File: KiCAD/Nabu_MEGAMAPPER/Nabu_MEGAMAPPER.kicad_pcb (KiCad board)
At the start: 2 copper layers, 41 parts, among them J1 Z80 Socket Header, J2 Z80 Socket Header, J3 JTAG, U1 Z80CPU, U10 74LS374, U11 74LS374, U12 74LS85, U13 XC9536PC44, U14 74LS139, U15 AS6C4008-55PCN, U16 AS6C4008-55PCN, U17 AS6C4008-55PCN, U18 AS6C4008-55PCN, U19 74LS245, U2 74LS32, U3 74LS670, U4 74LS670, U5 HM6116, U6 74LS157, U7 74LS157, U8 74LS157, U9 74LS244

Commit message: Continued work on PCB layout
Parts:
- moved J3 291.6 mm to (225.4, 78.1), turned to 180 degrees
- moved U15 271.8 mm to (139.7, 108.0)
- moved U5 269.7 mm to (207.6, 118.1)
- moved U9 267.7 mm to (167.0, 87.0), turned to 90 degrees
- moved C5 266.0 mm to (217.8, 114.9), turned to 180 degrees
- moved U19 255.8 mm to (186.7, 111.1)
- moved U2 246.0 mm to (167.0, 73.0), turned to 90 degrees
- moved C13 240.5 mm to (200.0, 92.7), turned to 90 degrees
- moved U16 234.0 mm to (118.1, 108.0)
- moved U10 223.9 mm to (134.0, 87.0), turned to 90 degrees
- moved C19 219.8 mm to (188.0, 107.9)
- moved C1 214.5 mm to (166.4, 94.6)
- moved U11 213.6 mm to (134.0, 73.0), turned to 90 degrees
- moved C2 213.6 mm to (163.8, 66.7), turned to -90 degrees
- moved U8 212.4 mm to (134.0, 101.0), turned to 90 degrees
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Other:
- board outline added: 156.8 x 86.4 mm
- board text added: "+5V"
- board text added: "GND"
- board text added: "Gavin Tersteeg, 2024"
- board text added: "Rev. 0"
- board text added: "TCK"
- board text added: "TDI"
- board text added: "TDO"
- board text added: "TMS"
- board text added: "Z80 MEGAMAPPER"

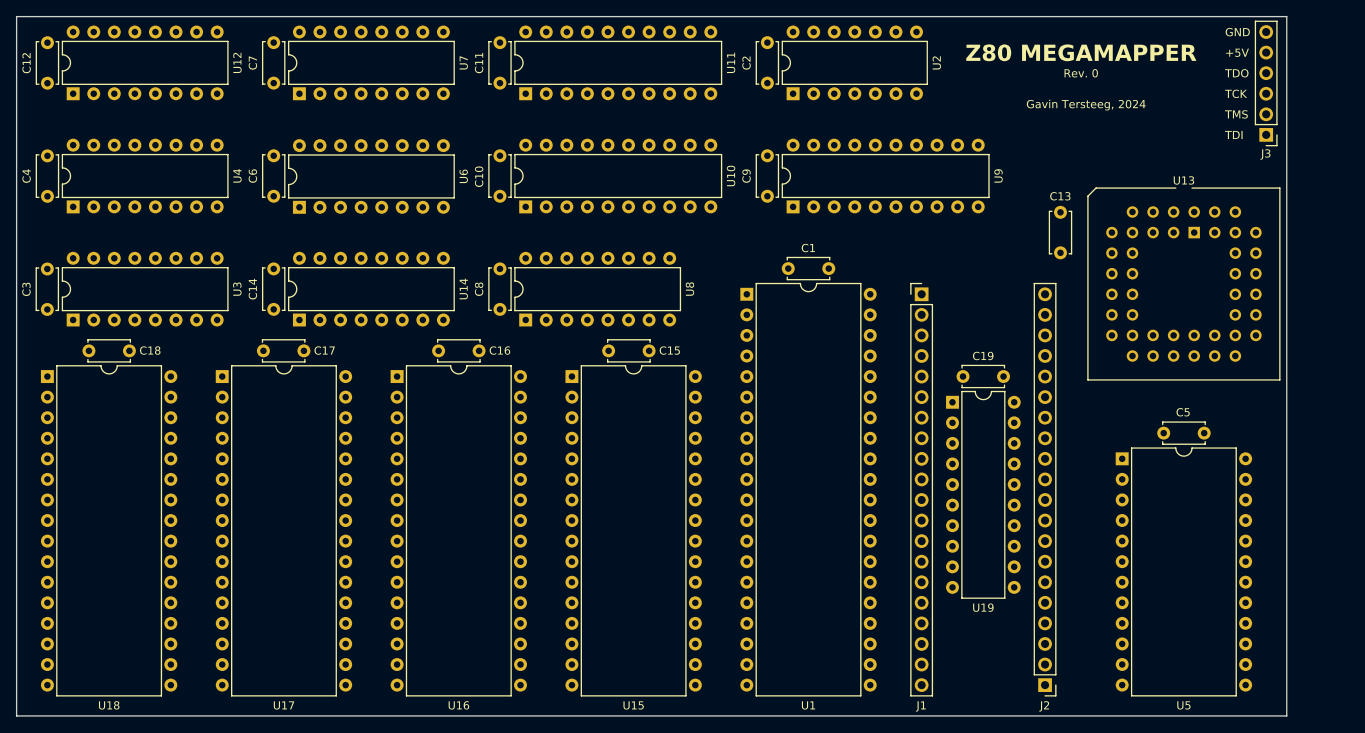
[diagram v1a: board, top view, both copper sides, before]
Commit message: Added bulk storage capacitor and started designing layout
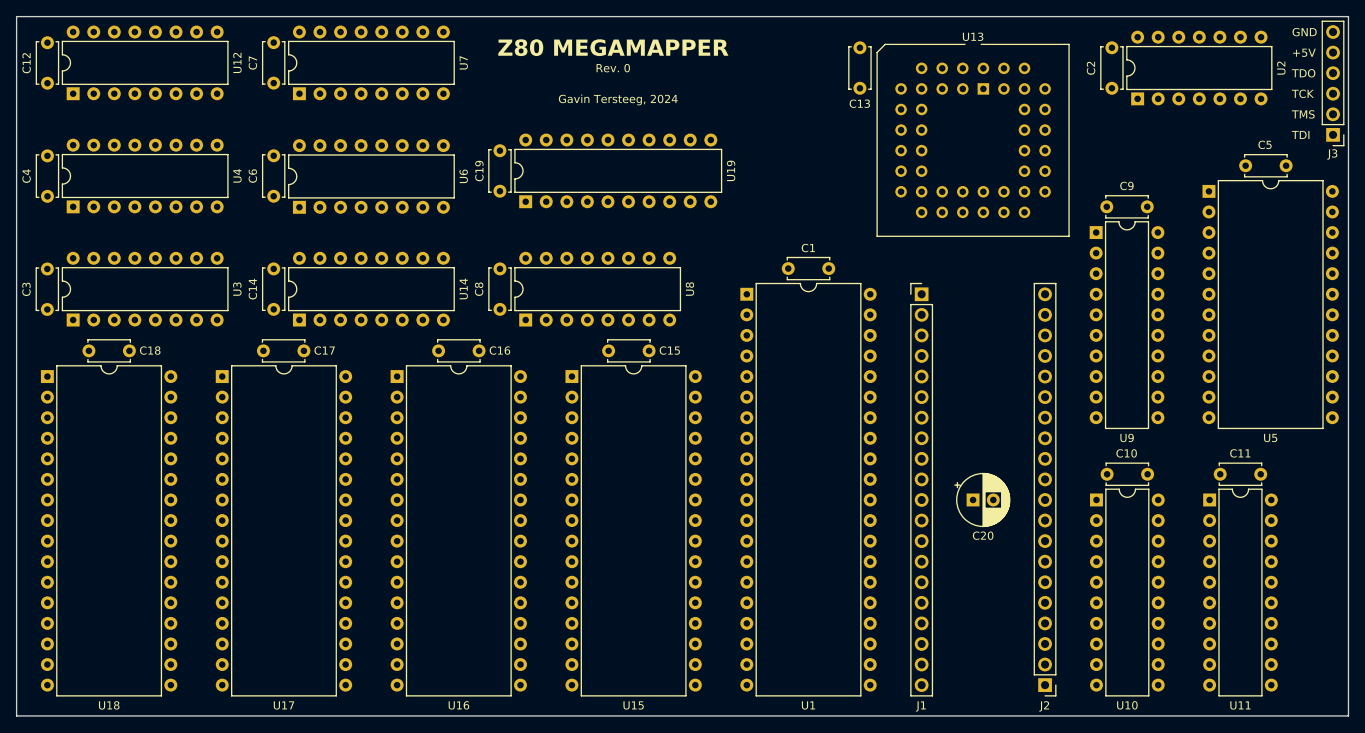
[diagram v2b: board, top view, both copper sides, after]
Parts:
- added C20: 100 uF, Capacitor_THT:CP_Radial_D6.3mm_P2.50mm, F.Cu at (189.2, 123.2)
- moved C11 108.0 mm to (224.8, 120.0), turned to 180 degrees
- moved U11 98.2 mm to (218.4, 123.2), turned to 0 degrees
- moved C10 89.1 mm to (210.8, 120.0), turned to 180 degrees
- moved U10 79.2 mm to (204.5, 123.2), turned to 0 degrees
- moved C19 61.6 mm to (130.8, 85.1), turned to 90 degrees
- moved U19 58.2 mm to (134.0, 86.4), turned to 90 degrees
- moved C9 47.3 mm to (210.7, 87.0), turned to 180 degrees
- moved U2 42.5 mm to (209.6, 73.7)
- moved C2 42.5 mm to (206.4, 67.3)
- moved U9 37.6 mm to (204.4, 90.2), turned to 0 degrees
- moved C13 35.4 mm to (175.3, 67.3), turned to -90 degrees
- moved U5 34.7 mm to (218.4, 85.1)
- moved C5 34.5 mm to (227.9, 81.9)
- moved U13 31.5 mm to (190.5, 72.4)
- moved J3 8.25 mm to (233.7, 78.1)
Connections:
- net /*XMEM_WR renamed Net-(U15-WE#)
- J2 pad 1: /*RD -> Net-(J2-Pin_1)
- U13 pad 25: /SYS_A14 -> /A14
- U13 pad 42: /SYS_A15 -> /A15
- U2 pad 4: GND -> /*RD
- U2 pad 5: GND -> /*RD
- U2 pad 6: unconnected-(U2-Pad6) -> Net-(J2-Pin_1)
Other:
- board size 156.8 x 86.4 mm -> 164.5 x 86.4 mm

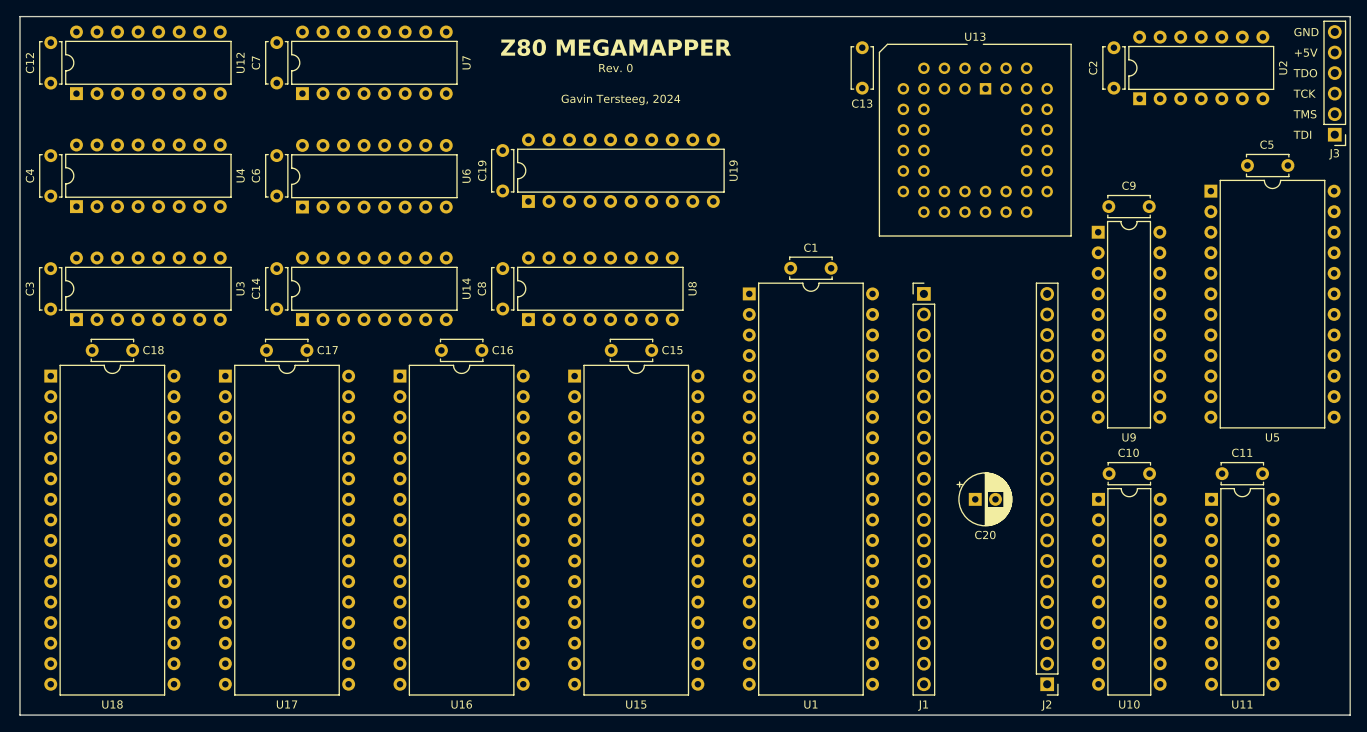
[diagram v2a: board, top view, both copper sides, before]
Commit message: Redid board layout for better routing
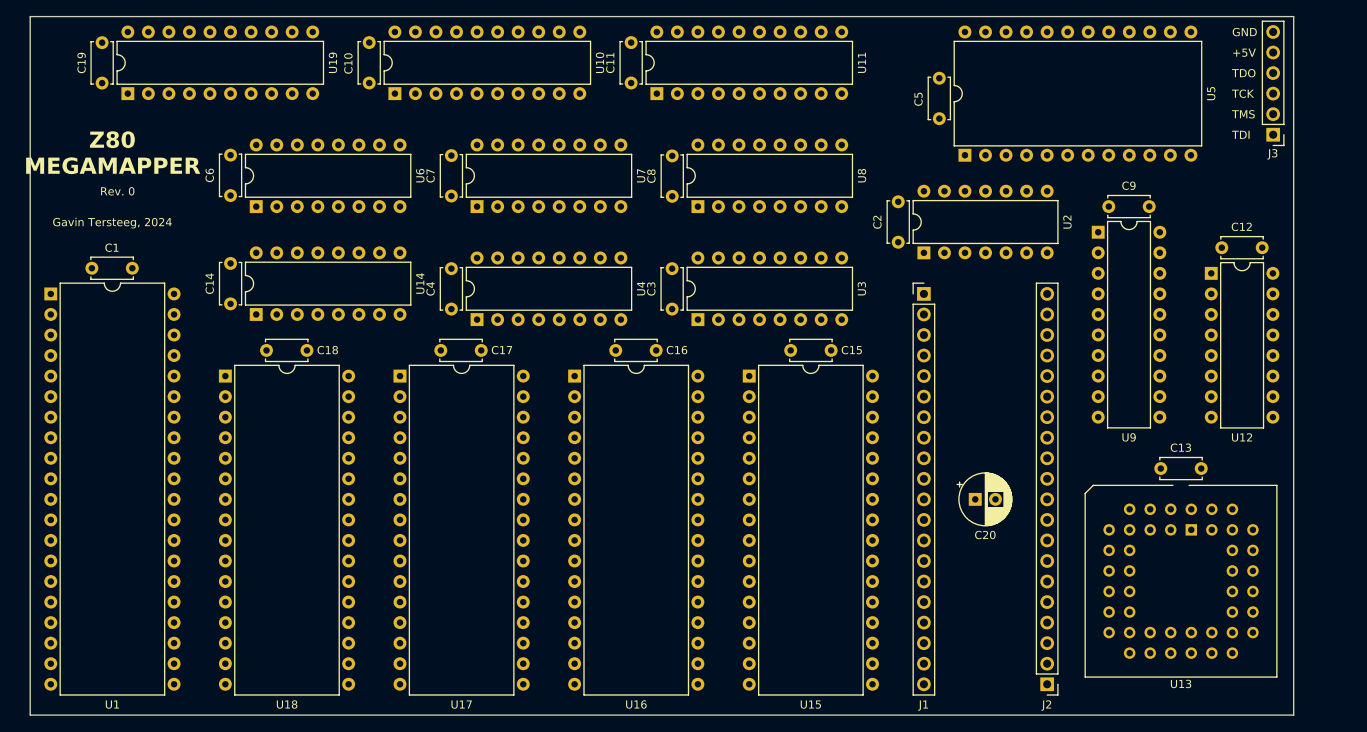
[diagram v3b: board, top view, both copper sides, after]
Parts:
- moved C12 151.9 mm to (224.7, 92.1), turned to 180 degrees
- moved U12 142.1 mm to (218.4, 95.2), turned to 0 degrees
- moved C10 110.2 mm to (114.3, 66.7), turned to -90 degrees
- moved U10 100.4 mm to (117.5, 73.0), turned to 90 degrees
- moved C11 94.5 mm to (146.7, 66.7), turned to -90 degrees
- moved C1 86.4 mm to (80.0, 94.6)
- moved U1 86.4 mm to (74.9, 97.8)
- moved U11 85.0 mm to (149.9, 73.0), turned to 90 degrees
- moved C3 76.8 mm to (151.8, 94.7)
- moved U3 76.8 mm to (154.9, 101.0)
- moved C13 66.8 mm to (217.2, 119.4), turned to 180 degrees
- moved U13 60.2 mm to (215.9, 127.0)
- moved U4 51.5 mm to (127.6, 101.0)
- moved C4 51.5 mm to (124.5, 94.7)
- moved U19 51.3 mm to (84.5, 73.0)
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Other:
- board size 164.5 x 86.4 mm -> 156.2 x 86.4 mm
